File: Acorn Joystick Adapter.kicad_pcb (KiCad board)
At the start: 2 copper layers, 67.9 x 52.1 mm, 31 parts, among them J1 Acorn Computer, J2 Atari #1, J3 Atari #2, Q1 BC337, Q2 BC337, Q3 BC337, Q4 BC337, Q5 BC337, Q6 BC337

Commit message: Added analog breakout header
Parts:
- added J4: Analog, Pin_Headers:Pin_Header_Straight_1x05_Pitch2.54mm, F.Cu at (126.7, 93.0)
- J1: footprint Connectors_DSub:DSUB-15_Male_Vertical_Pitch2.77x2.84mm -> RND_DSUB:DSUB-15_Male_Vertical_Pitch2.77x2.84mm
- J2, J3: footprint Connectors_DSub:DSUB-9_Male_Vertical_Pitch2.77x2.84mm -> RND_DSUB:DSUB-9_Male_Vertical_Pitch2.77x2.84mm
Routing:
- net A1_UP: track 56.9 -> 82.8 mm, vias 2 -> 3
- net A1_LEFT: track 64.2 -> 85.2 mm, vias 4 -> 5
- net A1_FIRE: track 19.5 -> 34.6 mm
- net VREF: track 143.8 -> 149.2 mm
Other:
- board text added: "+"
- board text added: "-"
- board text added: "Acorn Joystick Adapter Board Revision A https://hvetebolle.blogspot.com"
- board text added: "F"
- board text added: "X"
- board text added: "Y"
- board text removed: "https://hvetebolle.blogspot.com"

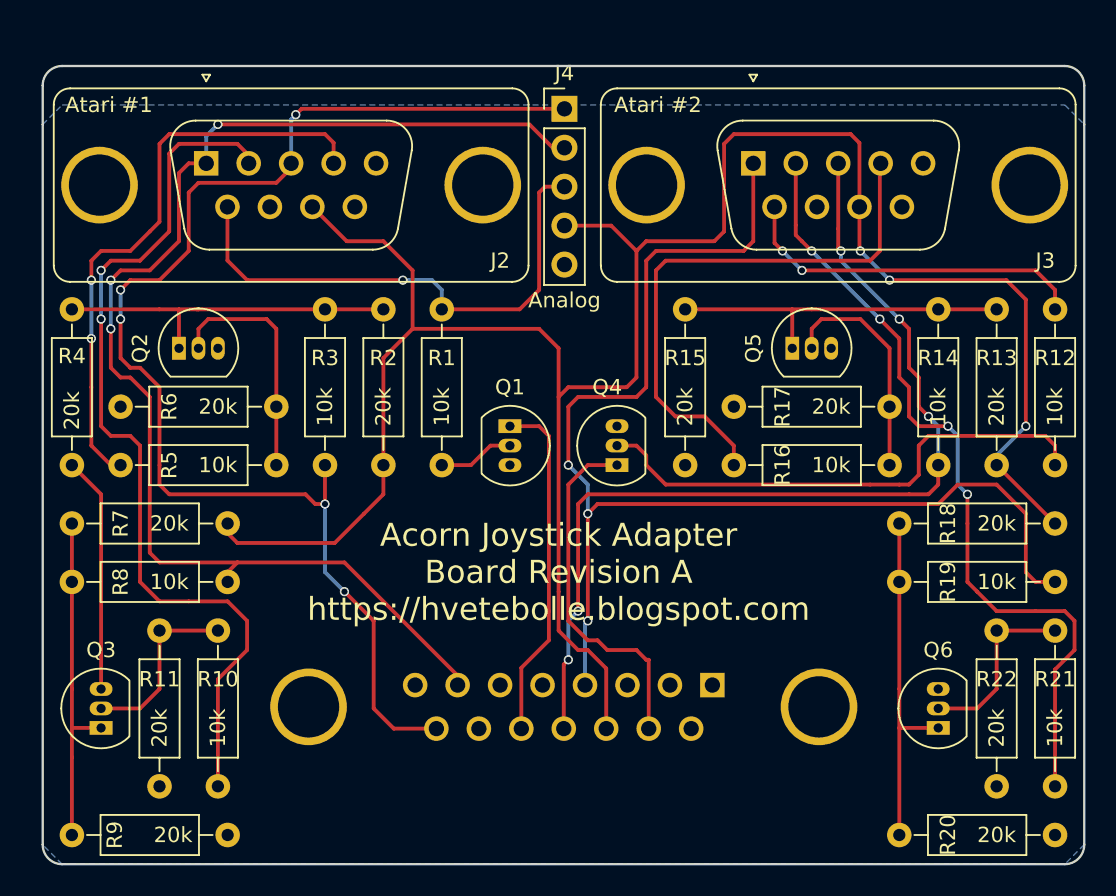
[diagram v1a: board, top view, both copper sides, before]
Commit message: Changed transistor footprint (easier to solder)
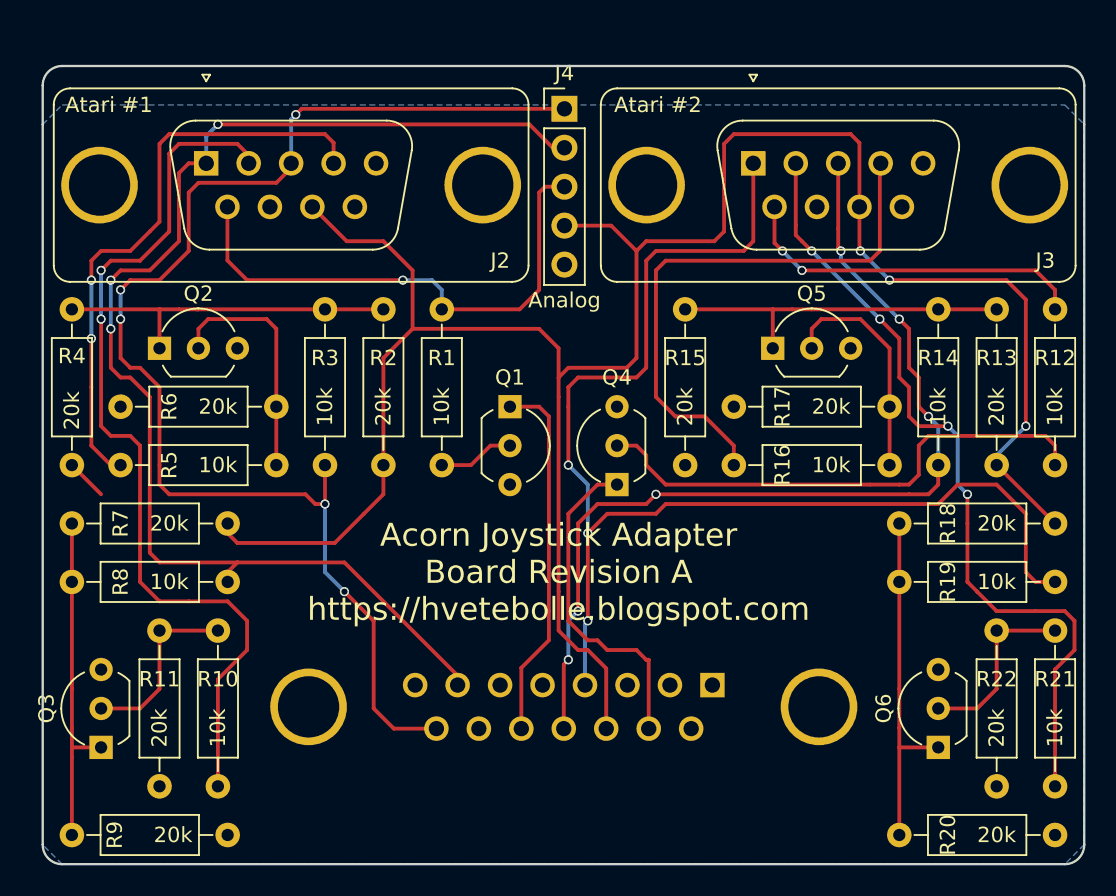
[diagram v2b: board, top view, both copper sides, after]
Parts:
- Q1, Q2, Q3, Q4, Q5, Q6: footprint TO_SOT_Packages_THT:TO-92_Inline_Narrow_Oval -> TO_SOT_Packages_THT:TO-92_Inline_Wide
- moved Q1 1.27 mm to (123.2, 112.4)
- moved Q3 1.27 mm to (96.5, 134.6)
- moved Q6 1.27 mm to (151.1, 134.6)
- moved Q2 1.27 mm to (100.3, 108.6)
- moved Q4 1.27 mm to (130.2, 117.5)
- moved Q5 1.27 mm to (140.3, 108.6)
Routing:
- net GNDA: track 15.4 -> 2.69 mm
- net B_PB1: track 23.4 -> 21.7 mm
- net B_PB0: track 22.6 -> 23.9 mm
- net VREF: track 149.2 -> 148.0 mm
- net A2_LEFT: track 62.7 -> 62.0 mm, vias 5 -> 6
- net A2_UP: track 81.3 -> 81.9 mm

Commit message: Rotated atari connectors so 90 degree ones can be used
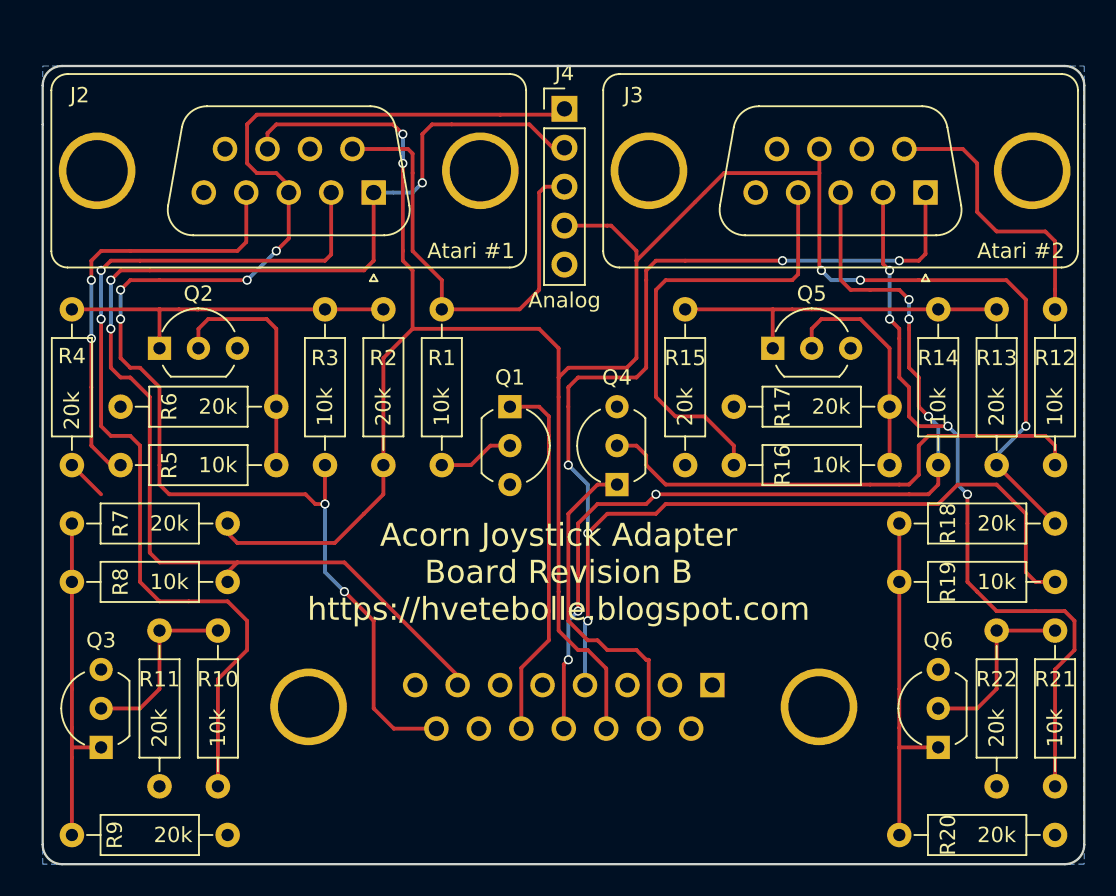
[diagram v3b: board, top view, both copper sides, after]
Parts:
- moved J3 11.4 mm to (150.3, 98.4), turned to 180 degrees
- moved J2 11.1 mm to (114.3, 98.4), turned to 180 degrees
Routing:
- net A1_RIGHT: track 38.3 -> 28.3 mm
- net A2_UP: track 81.9 -> 91.3 mm, vias 3 -> 5
- net VREF: track 148.0 -> 155.1 mm, vias 3 -> 5
- net A2_RIGHT: track 36.8 -> 29.7 mm
- net A1_LEFT: track 85.2 -> 90.1 mm, vias 5 -> 6
- net A2_FIRE: track 23.2 -> 18.6 mm, vias 2 -> 0
- net A1_FIRE: track 34.6 -> 30.0 mm, vias 1 -> 0
- net A2_DOWN: track 52.4 -> 48.2 mm
- net A1_DOWN: track 58.6 -> 61.2 mm
- net A1_UP: track 82.8 -> 83.7 mm
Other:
- board text added: "Acorn Joystick Adapter Board Revision B"
- board text added: "Acorn Joystick Adapter Board Revision B https://hvetebolle.blogspot.com"
- board text removed: "Acorn Joystick Adapter Board Revision A"
- board text removed: "Acorn Joystick Adapter Board Revision A https://hvetebolle.blogspot.com"

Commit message: Smaller DSUB mounting holes
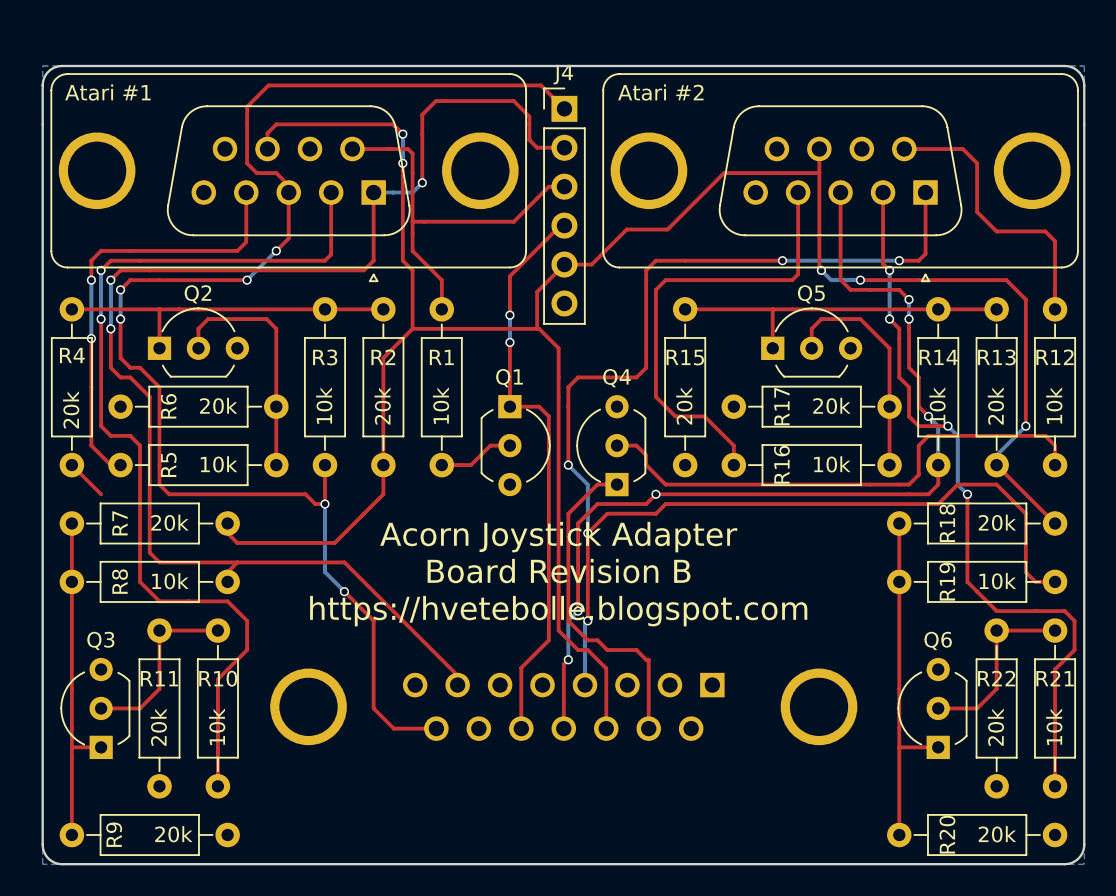
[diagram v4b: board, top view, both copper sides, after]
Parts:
- J4: footprint Pin_Headers:Pin_Header_Straight_1x05_Pitch2.54mm -> Pin_Headers:Pin_Header_Straight_1x06_Pitch2.54mm
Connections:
- J4 pad 4: VREF -> B_PB0
- J4 pad 5: GNDA -> VREF
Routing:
- net B_PB0: track 23.9 -> 37.3 mm, vias 0 -> 2
- net VREF: track 155.1 -> 146.9 mm
- net A1_FIRE: track 30.0 -> 25.9 mm
- net A1_UP: track 83.7 -> 87.3 mm
- net A1_LEFT: track 90.1 -> 92.0 mm

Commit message: Upgrade schematic to new KiCAD
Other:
- net class Default removed
- board text added: "Acorn Joystick Adapter"
- board text added: "Acorn Joystick Adapter Board Revision C github.com/tebl"
- board text removed: "Acorn Joystick Adapter Board Revision B"
- board text removed: "Acorn Joystick Adapter Board Revision B https://hvetebolle.blogspot.com"

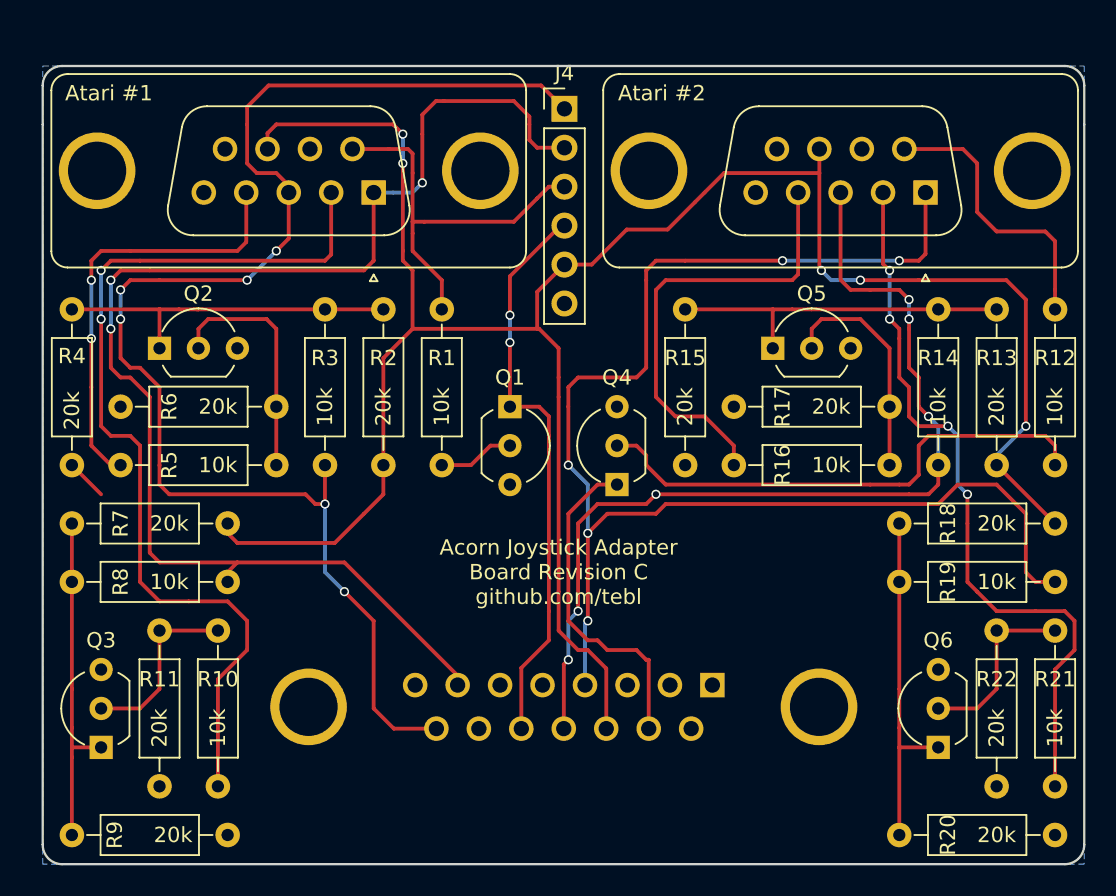
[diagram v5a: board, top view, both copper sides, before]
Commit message: Updated project for recent version of KiCAD
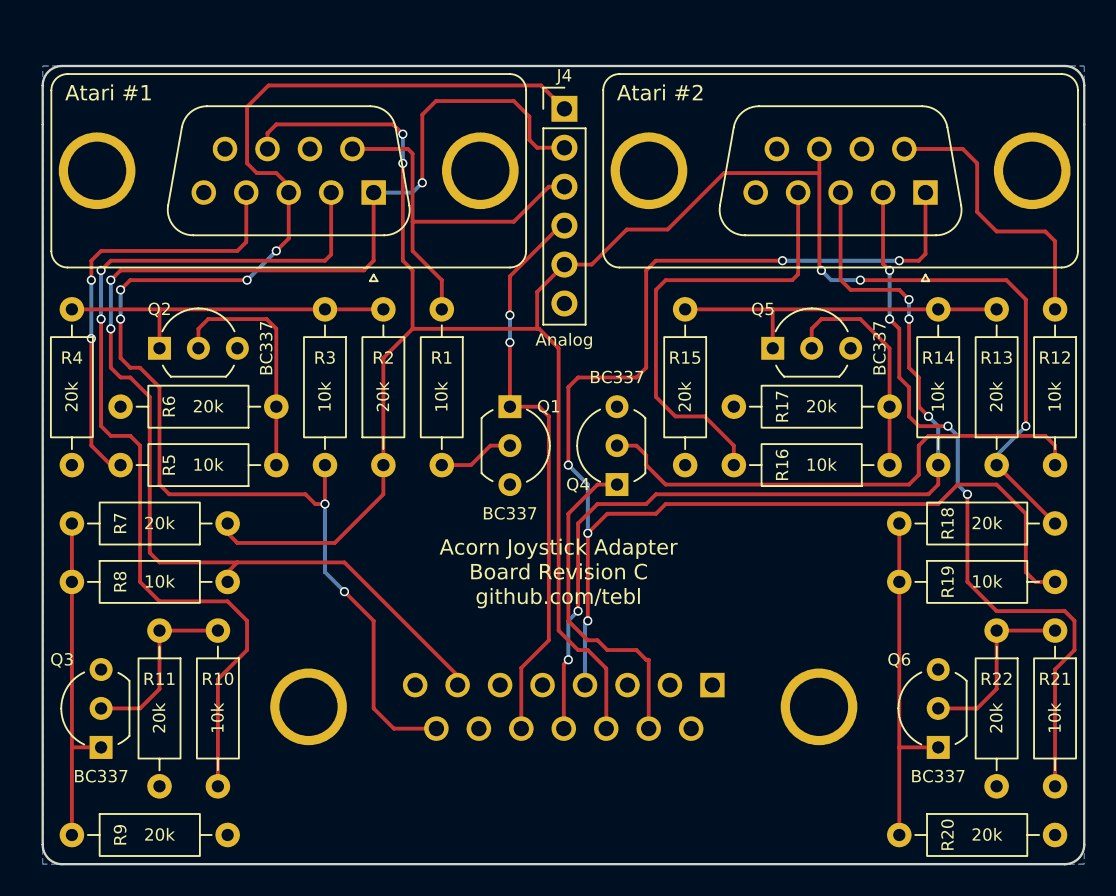
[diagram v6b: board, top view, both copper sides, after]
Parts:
- J4: footprint Pin_Headers:Pin_Header_Straight_1x06_Pitch2.54mm -> Connector_PinHeader_2.54mm:PinHeader_1x06_P2.54mm_Vertical
- Q1, Q2, Q3, Q4, Q5, Q6: footprint TO_SOT_Packages_THT:TO-92_Inline_Wide -> Package_TO_SOT_THT:TO-92_Inline_Wide
- R1, R10, R11, R12, R13, R14, R15, R16, R17, R18, R19, R2, R20, R21, R22, R3, R4, R5, R6, R7, R8, R9: footprint Resistors_THT:R_Axial_DIN0207_L6.3mm_D2.5mm_P10.16mm_Horizontal -> Resistor_THT:R_Axial_DIN0207_L6.3mm_D2.5mm_P10.16mm_Horizontal
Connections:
- J1 pad 1: (no net) -> unconnected-(J1-Pad1)
- J1 pad 14: (no net) -> unconnected-(J1-P14-Pad14)
- J1 pad 2: (no net) -> unconnected-(J1-Pad2)
- J1 pad 3: (no net) -> unconnected-(J1-Pad3)
- J1 pad 5: (no net) -> unconnected-(J1-Pad5)
- J1 pad 6: (no net) -> unconnected-(J1-Pad6)
- J1 pad 9: (no net) -> unconnected-(J1-P9-Pad9)
- J2 pad 5: (no net) -> unconnected-(J2-Pad5)
- J2 pad 7: (no net) -> unconnected-(J2-Pad7)
- J2 pad 9: (no net) -> unconnected-(J2-Pad9)
- J3 pad 5: (no net) -> unconnected-(J3-Pad5)
- J3 pad 7: (no net) -> unconnected-(J3-Pad7)
- J3 pad 9: (no net) -> unconnected-(J3-Pad9)
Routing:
- net GNDA: track 2.69 -> 0.00 mm
- net A1_UP: track 87.3 -> 86.6 mm
- net A2_LEFT: vias 6 -> 5
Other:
- rule pad_to_mask_clearance: 0.2 -> 0
